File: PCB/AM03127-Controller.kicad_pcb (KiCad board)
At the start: 2 copper layers, 23 x 76 mm, 13 parts, among them U1 XIAO-ESP32-C3-DIP, U2 MAX3232, U3 AMS1117 5.0

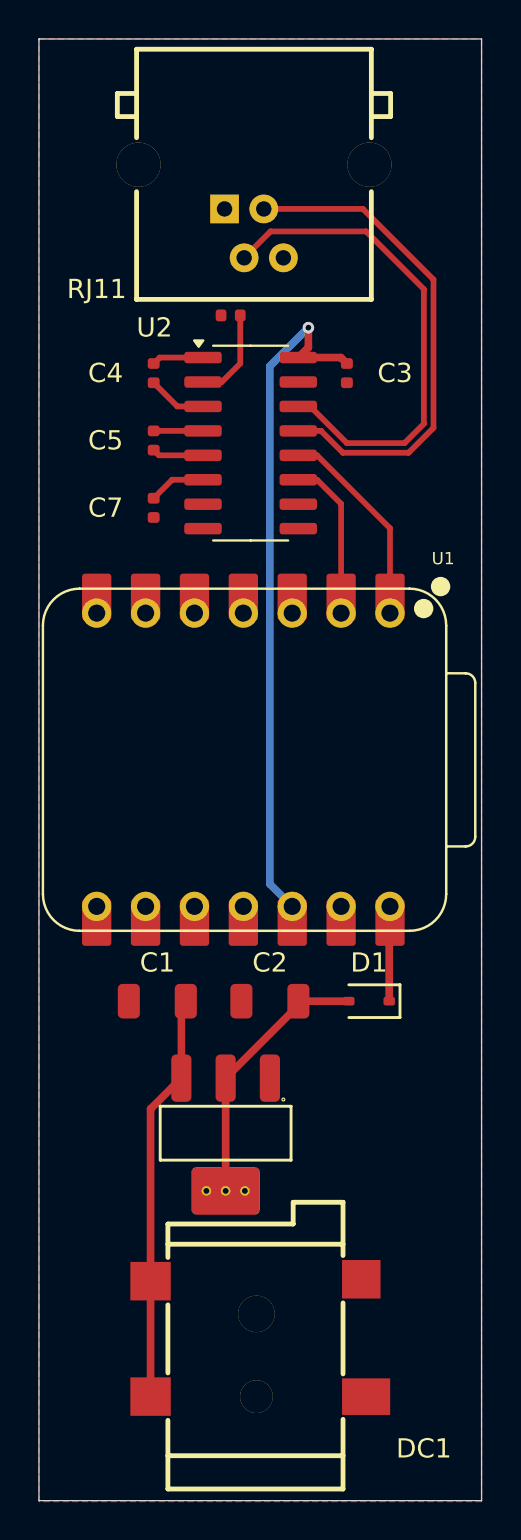
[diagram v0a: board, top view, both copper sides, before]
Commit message: Refactor LDO to Buckconverter
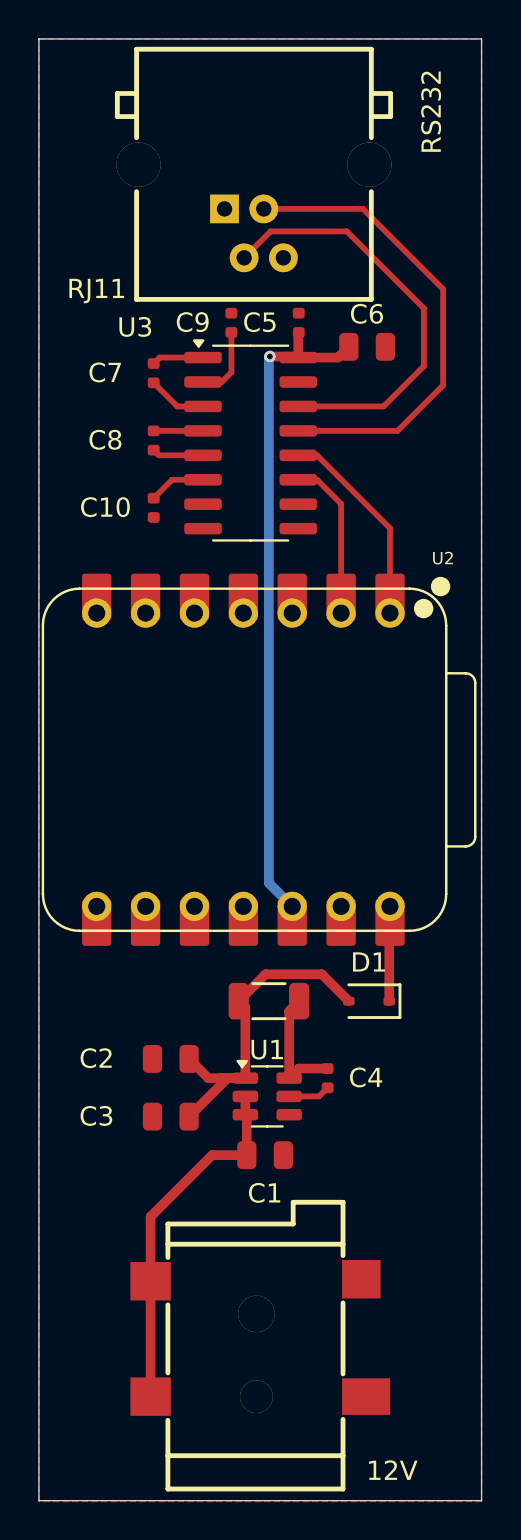
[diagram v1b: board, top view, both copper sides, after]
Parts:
- removed the U3 at (133.7, 124.9)
- added C3: 22uF, PCM_JLCPCB:C_0805, F.Cu at (130.8, 124.0)
- added C4: 100nF, PCM_JLCPCB:C_0402, F.Cu at (139.0, 122.0)
- added C6: 10uF, PCM_JLCPCB:C_0805, F.Cu at (141.1, 84.0)
- added L1: 10uH,25mA, PCM_JLCPCB:L_1206, F.Cu at (135.9, 118.0)
- added U1: AP63205WU, Package_TO_SOT_SMD:TSOT-23-6, F.Cu at (135.9, 123.0)
- C1, C2: footprint PCM_JLCPCB:C_1206 -> PCM_JLCPCB:C_0805
- moved C1 9.77 mm to (135.8, 126.0), turned to 0 degrees
- moved C2 5.96 mm to (130.8, 121.0)
- moved C5 3.62 mm to (137.5, 82.8), turned to 90 degrees
- moved C9 0.39 mm to (134.0, 82.8), turned to 90 degrees
- renumbered C7 to C10, C3 to C5, C4 to C7, C5 to C8, C6 to C9, U1 to U2, U2 to U3
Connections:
- net Net-(C2-Pad1) renamed /BuckFeedback
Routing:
- net /BuckOut: track 0.00 -> 6.42 mm
- net /BuckFeedback: track 14.0 -> 19.4 mm
- net /RS232 TX: track 26.5 -> 22.6 mm
- net +12V: track 21.3 -> 18.8 mm
- net Net-(U1-SW): track 0.00 -> 2.19 mm
- net /RS232 RX: track 26.1 -> 24.6 mm
- net Net-(U3-VS+): track 4.83 -> 3.76 mm
- net /UART RX: track 12.6 -> 11.6 mm
- net +3.3V: track 36.6 -> 35.7 mm
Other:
- board text added: "12V"
- board text added: "RS232"

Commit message: Refactor PCB using buttom GND Plate
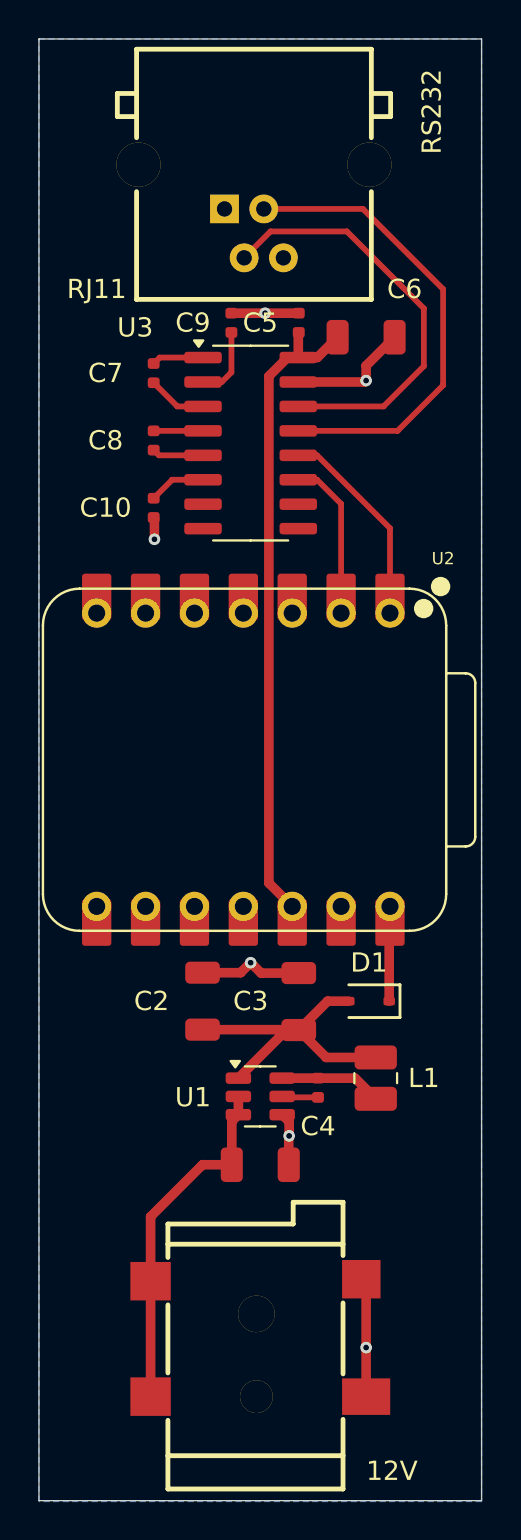
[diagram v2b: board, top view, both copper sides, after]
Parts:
- C1, C6: value 10uF -> 22uF; footprint PCM_JLCPCB:C_0805 -> PCM_JLCPCB:C_1206
- C2, C3: footprint PCM_JLCPCB:C_0805 -> PCM_JLCPCB:C_1206
- L1: value 10uH,25mA -> 4.7uH; footprint PCM_JLCPCB:L_1206 -> Inductor_SMD:L_1008_2520Metric
- moved C3 8.94 mm to (137.5, 118.0), turned to 90 degrees
- moved L1 6.84 mm to (141.5, 122.0), turned to 90 degrees
- moved C2 3.42 mm to (132.5, 118.0), turned to 90 degrees
- moved C4 0.71 mm to (138.5, 122.5)
- moved C1 0.56 mm to (135.5, 126.5)
- moved C6 0.50 mm to (141.0, 83.5)
- moved U1 0.36 mm to (135.5, 123.0)
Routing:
- net GND: track 0.53 -> 26.0 mm, vias 0 -> 6
- net /BuckFeedback: track 19.4 -> 17.0 mm
- net /BuckOut: track 6.42 -> 5.31 mm
- net +3.3V: track 35.7 -> 34.8 mm, vias 1 -> 0
- added copper zone on B.Cu, net GND
- removed copper zone on F.Cu, net GND
